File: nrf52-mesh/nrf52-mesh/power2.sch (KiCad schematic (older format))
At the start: 2 parts

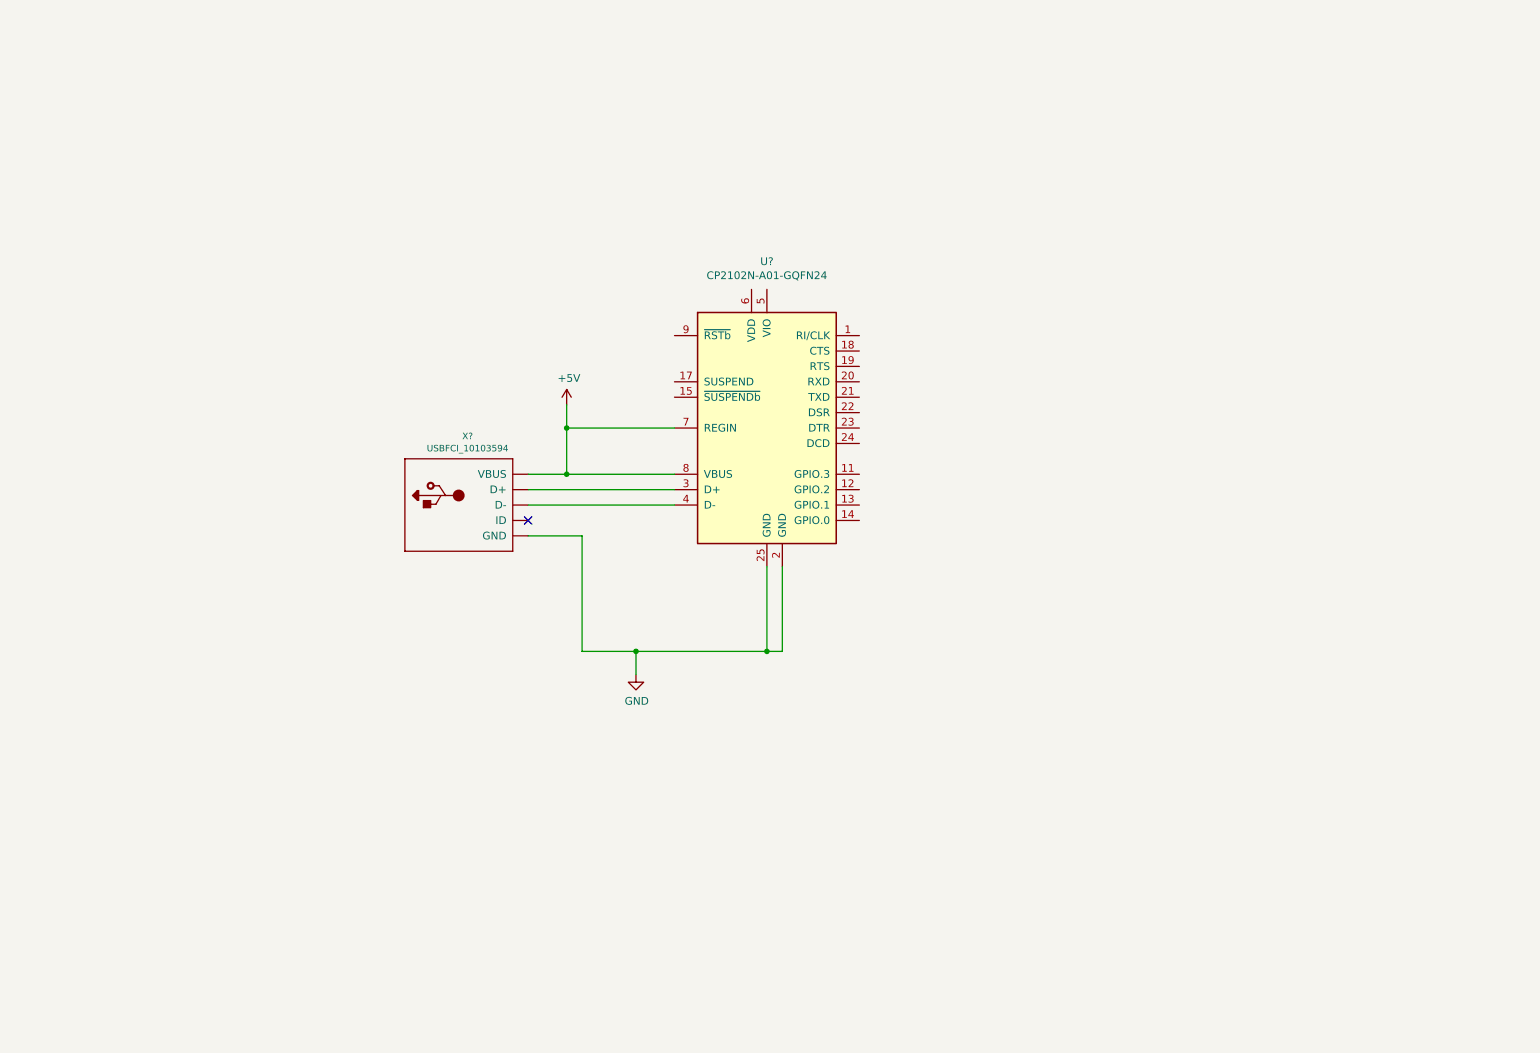
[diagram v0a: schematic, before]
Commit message: CP2102N + MAX1555 + FAN5341 + TPS560200 + TLV62568
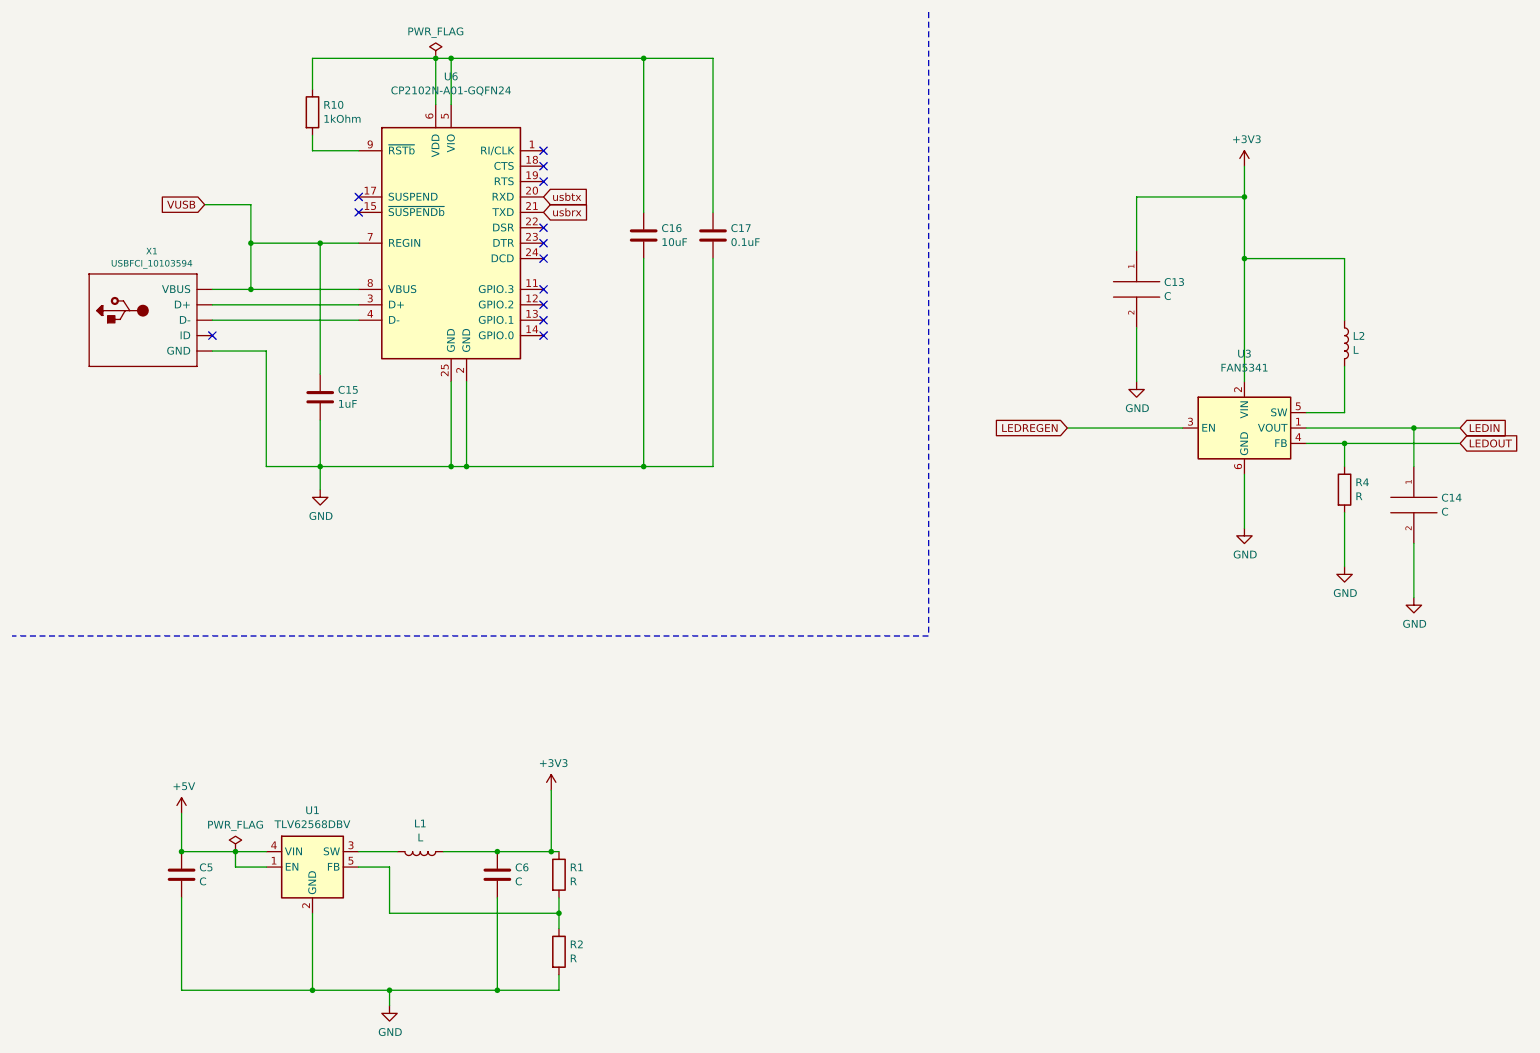
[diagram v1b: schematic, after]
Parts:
- added C13, C14: C, symbol pspice:C
- added C15: 1uF, symbol Device:C
- added C16: 10uF, symbol Device:C
- added C17: 0.1uF, symbol Device:C
- added C5, C6: C, symbol Device:C
- added L1, L2: L, symbol Device:L
- added R1, R2, R4: R, symbol Device:R
- added R10: 1kOhm, symbol Device:R
- added U1: TLV62568DBV, Package_TO_SOT_SMD:SOT-23-5, symbol Regulator_Switching:TLV62568DBV
- added U3: FAN5341, kifootp:FAN5341, symbol kilib:FAN5341
- X1: renamed from X?; footprint (none) -> kifootp:FCI_10103594_MILL
- gave numbers to parts that had none: 1
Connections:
- net +5V: now also C5.1, U1.1 (EN), U1.4 (VIN); no longer U6.7 (REGIN), U6.8 (VBUS), X1.VBUS
- net GND: now also C13.2, C14.2, C15.2, C16.2, C17.2, C5.2, C6.2, R2.2, R4.2, U1.2 (GND), U3.6 (GND)
- net usbtx: now reaches U6.20 (RXD)
- net usbrx: now reaches U6.21 (TXD)
- net at U6.5 (VIO): now also U6.6 (VDD), C16.1, C17.1, R10.1
- net at U6.9 (~RSTb): now also R10.2
- new net: L1.2, U1.3 (SW)
- new net: R1.2, R2.1, U1.5 (FB)
- new net: L2.2, U3.5 (SW)
- new net +3V3: C13.1, C6.1, L1.1, L2.1, R1.1, U3.2 (VIN)
- new net LEDIN: C14.1, U3.1 (VOUT)
- new net LEDOUT: R4.1, U3.4 (FB)
- new net LEDREGEN: U3.3 (EN)
- new net VUSB: C15.1, U6.7 (REGIN), U6.8 (VBUS), X1.VBUS
- no-connect marks 1 -> 13
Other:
- moved on the sheet: U6, X1

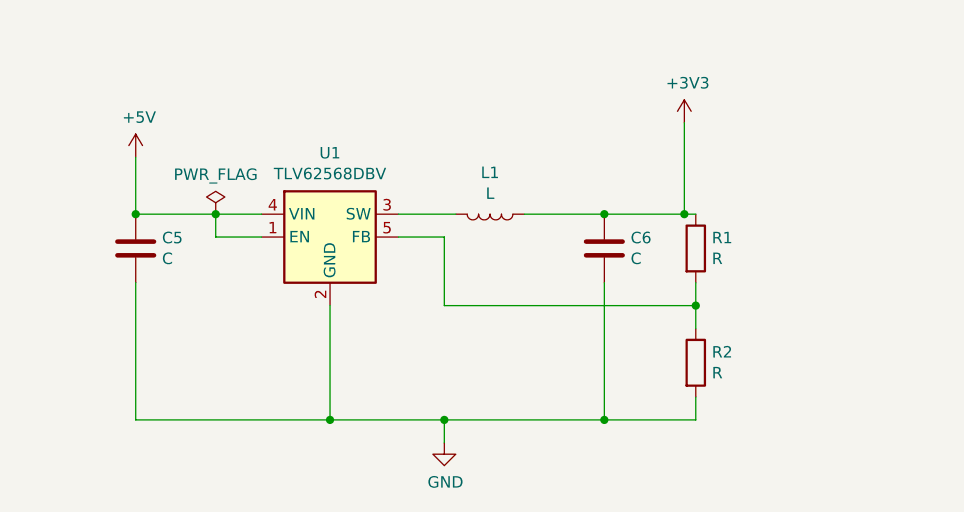
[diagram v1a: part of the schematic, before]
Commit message: CP2102N + MAX1555 + FAN5341 + TPS560200 + TLV62568
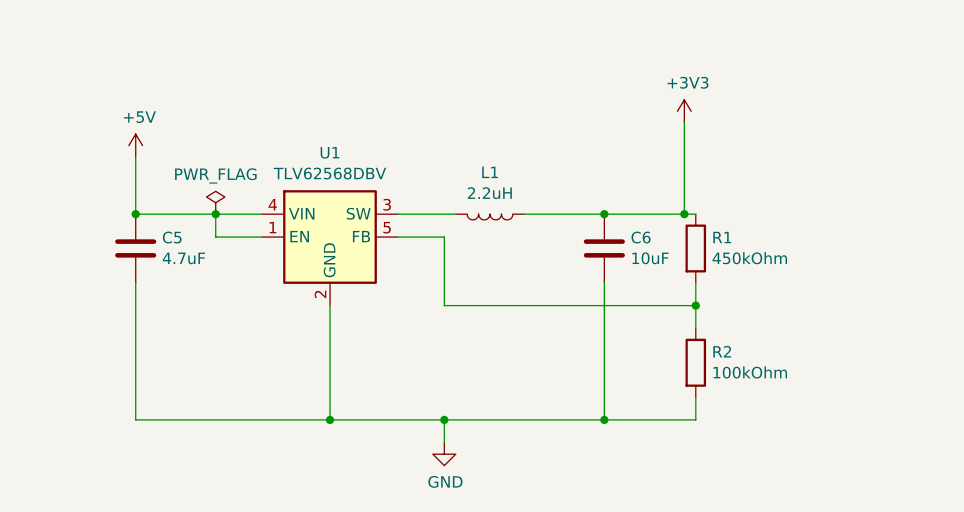
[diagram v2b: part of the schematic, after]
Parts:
- C5: value C -> 4.7uF
- C6: value C -> 10uF
- L1: value L -> 2.2uH
- R1: value R -> 450kOhm
- R2: value R -> 100kOhm
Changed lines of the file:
@@
 AR Path="/5E4F8472/5E5B7E4C" Ref="C5"  Part="1"
 F 0 "C5" H 1765 6196 50  0000 L CNN
-F 1 "C" H 1765 6105 50  0000 L CNN
+F 1 "4.7uF" H 1765 6105 50  0000 L CNN
 F 2 "" H 1688 6000 50  0001 C CNN
 F 3 "~" H 1650 6150 50  0001 C CNN
@@
 AR Path="/5E4F8472/5E5B7E52" Ref="L1"  Part="1"
 F 0 "L1" V 3019 6000 50  0000 C CNN
-F 1 "L" V 3110 6000 50  0000 C CNN
+F 1 "2.2uH" V 3110 6000 50  0000 C CNN
 F 2 "" H 3200 6000 50  0001 C CNN
 F 3 "~" H 3200 6000 50  0001 C CNN
@@
 AR Path="/5E4F8472/5E5B7E58" Ref="C6"  Part="1"
 F 0 "C6" H 3815 6196 50  0000 L CNN
-F 1 "C" H 3815 6105 50  0000 L CNN
+F 1 "10uF" H 3815 6105 50  0000 L CNN
 F 2 "" H 3738 6000 50  0001 C CNN
 F 3 "~" H 3700 6150 50  0001 C CNN
@@
 AR Path="/5E4F8472/5E5B7E5E" Ref="R1"  Part="1"
 F 0 "R1" H 4170 6196 50  0000 L CNN
-F 1 "R" H 4170 6105 50  0000 L CNN
+F 1 "450kOhm" H 4170 6105 50  0000 L CNN
 F 2 "" V 4030 6150 50  0001 C CNN
 F 3 "~" H 4100 6150 50  0001 C CNN
@@
 AR Path="/5E4F8472/5E5B7E64" Ref="R2"  Part="1"
 F 0 "R2" H 4170 6696 50  0000 L CNN
-F 1 "R" H 4170 6605 50  0000 L CNN
+F 1 "100kOhm" H 4170 6605 50  0000 L CNN
 F 2 "" V 4030 6650 50  0001 C CNN
 F 3 "~" H 4100 6650 50  0001 C CNN

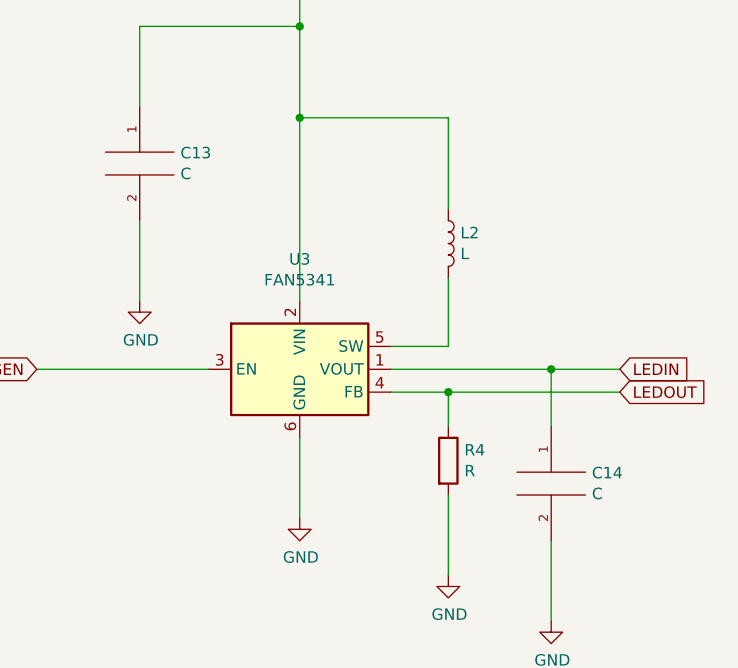
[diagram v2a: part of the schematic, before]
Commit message: CP2102N + MAX1555 + FAN5341 + TPS560200 + TLV62568
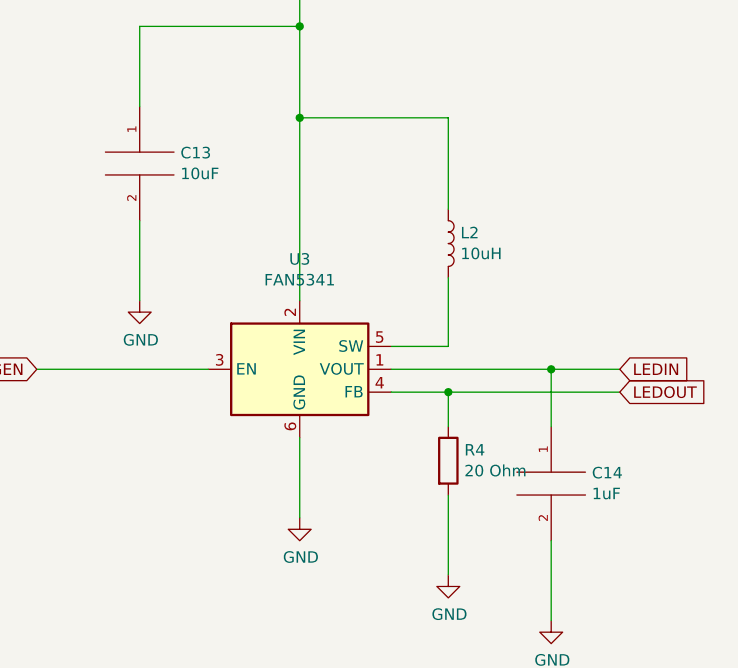
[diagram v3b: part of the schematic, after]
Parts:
- C13: value C -> 10uF; footprint (none) -> Capacitor_SMD:C_0603_1608Metric
- C14: value C -> 1uF; footprint (none) -> Capacitor_SMD:C_0402_1005Metric
- C15, C17, C5, C6: footprint (none) -> Capacitor_SMD:C_0402_1005Metric
- C16: footprint (none) -> Capacitor_SMD:C_0603_1608Metric
- L2: value L -> 10uH
- R1, R10, R2: footprint (none) -> Resistor_SMD:R_0402_1005Metric
- R4: value R -> 20 Ohm; footprint (none) -> Resistor_SMD:R_0402_1005Metric
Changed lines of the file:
@@
 F 0 "C5" H 1765 6196 50  0000 L CNN
 F 1 "4.7uF" H 1765 6105 50  0000 L CNN
-F 2 "" H 1688 6000 50  0001 C CNN
+F 2 "Capacitor_SMD:C_0402_1005Metric" H 1688 6000 50  0001 C CNN
 F 3 "~" H 1650 6150 50  0001 C CNN
 	1    1650 6150
@@
 F 0 "C6" H 3815 6196 50  0000 L CNN
 F 1 "10uF" H 3815 6105 50  0000 L CNN
-F 2 "" H 3738 6000 50  0001 C CNN
+F 2 "Capacitor_SMD:C_0402_1005Metric" H 3738 6000 50  0001 C CNN
 F 3 "~" H 3700 6150 50  0001 C CNN
 	1    3700 6150
@@
 F 0 "R1" H 4170 6196 50  0000 L CNN
 F 1 "450kOhm" H 4170 6105 50  0000 L CNN
-F 2 "" V 4030 6150 50  0001 C CNN
+F 2 "Resistor_SMD:R_0402_1005Metric" V 4030 6150 50  0001 C CNN
 F 3 "~" H 4100 6150 50  0001 C CNN
 	1    4100 6150
@@
 F 0 "R2" H 4170 6696 50  0000 L CNN
 F 1 "100kOhm" H 4170 6605 50  0000 L CNN
-F 2 "" V 4030 6650 50  0001 C CNN
+F 2 "Resistor_SMD:R_0402_1005Metric" V 4030 6650 50  0001 C CNN
 F 3 "~" H 4100 6650 50  0001 C CNN
 	1    4100 6650
@@
 AR Path="/5E4F8472/5E5C2A77" Ref="C14"  Part="1"
 F 0 "C14" H 9828 3796 50  0000 L CNN
-F 1 "C" H 9828 3705 50  0000 L CNN
-F 2 "" H 9650 3750 50  0001 C CNN
+F 1 "1uF" H 9828 3705 50  0000 L CNN
+F 2 "Capacitor_SMD:C_0402_1005Metric" H 9650 3750 50  0001 C CNN
 F 3 "~" H 9650 3750 50  0001 C CNN
 	1    9650 3750
@@
 AR Path="/5E4F8472/5E5C2A7D" Ref="R4"  Part="1"
 F 0 "R4" H 9270 3696 50  0000 L CNN
-F 1 "R" H 9270 3605 50  0000 L CNN
-F 2 "" V 9130 3650 50  0001 C CNN
+F 1 "20 Ohm" H 9270 3605 50  0000 L CNN
+F 2 "Resistor_SMD:R_0402_1005Metric" V 9130 3650 50  0001 C CNN
 F 3 "~" H 9200 3650 50  0001 C CNN
 	1    9200 3650
@@
 AR Path="/5E4F8472/5E5C2A9B" Ref="C13"  Part="1"
 F 0 "C13" H 8028 2396 50  0000 L CNN
-F 1 "C" H 8028 2305 50  0000 L CNN
-F 2 "" H 7850 2350 50  0001 C CNN
+F 1 "10uF" H 8028 2305 50  0000 L CNN
+F 2 "Capacitor_SMD:C_0603_1608Metric" H 7850 2350 50  0001 C CNN
 F 3 "~" H 7850 2350 50  0001 C CNN
 	1    7850 2350
@@
 AR Path="/5E4F8472/5E5C2AA1" Ref="L2"  Part="1"
 F 0 "L2" H 9253 2746 50  0000 L CNN
-F 1 "L" H 9253 2655 50  0000 L CNN
+F 1 "10uH" H 9253 2655 50  0000 L CNN
 F 2 "" H 9200 2700 50  0001 C CNN
 F 3 "~" H 9200 2700 50  0001 C CNN
@@
 F 0 "R10" H 2570 1246 50  0000 L CNN
 F 1 "1kOhm" H 2570 1155 50  0000 L CNN
-F 2 "" V 2430 1200 50  0001 C CNN
+F 2 "Resistor_SMD:R_0402_1005Metric" V 2430 1200 50  0001 C CNN
 F 3 "~" H 2500 1200 50  0001 C CNN
 	1    2500 1200
@@
 F 0 "C15" H 2665 3096 50  0000 L CNN
 F 1 "1uF" H 2665 3005 50  0000 L CNN
-F 2 "" H 2588 2900 50  0001 C CNN
+F 2 "Capacitor_SMD:C_0402_1005Metric" H 2588 2900 50  0001 C CNN
 F 3 "~" H 2550 3050 50  0001 C CNN
 	1    2550 3050
@@
 F 0 "C16" H 4765 2046 50  0000 L CNN
 F 1 "10uF" H 4765 1955 50  0000 L CNN
-F 2 "" H 4688 1850 50  0001 C CNN
+F 2 "Capacitor_SMD:C_0603_1608Metric" H 4688 1850 50  0001 C CNN
 F 3 "~" H 4650 2000 50  0001 C CNN
 	1    4650 2000
@@
 F 0 "C17" H 5215 2046 50  0000 L CNN
 F 1 "0.1uF" H 5215 1955 50  0000 L CNN
-F 2 "" H 5138 1850 50  0001 C CNN
+F 2 "Capacitor_SMD:C_0402_1005Metric" H 5138 1850 50  0001 C CNN
 F 3 "~" H 5100 2000 50  0001 C CNN
 	1    5100 2000

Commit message: CP2102N + MAX1555 + FAN5341 + TPS560200 + TLV62568
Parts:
- L1, L2: footprint (none) -> Inductor_SMD:L_0805_2012Metric
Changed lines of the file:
@@
 F 0 "L1" V 3019 6000 50  0000 C CNN
 F 1 "2.2uH" V 3110 6000 50  0000 C CNN
-F 2 "" H 3200 6000 50  0001 C CNN
+F 2 "Inductor_SMD:L_0805_2012Metric" H 3200 6000 50  0001 C CNN
 F 3 "~" H 3200 6000 50  0001 C CNN
 	1    3200 6000
@@
 F 0 "L2" H 9253 2746 50  0000 L CNN
 F 1 "10uH" H 9253 2655 50  0000 L CNN
-F 2 "" H 9200 2700 50  0001 C CNN
+F 2 "Inductor_SMD:L_0805_2012Metric" H 9200 2700 50  0001 C CNN
 F 3 "~" H 9200 2700 50  0001 C CNN
 	1    9200 2700

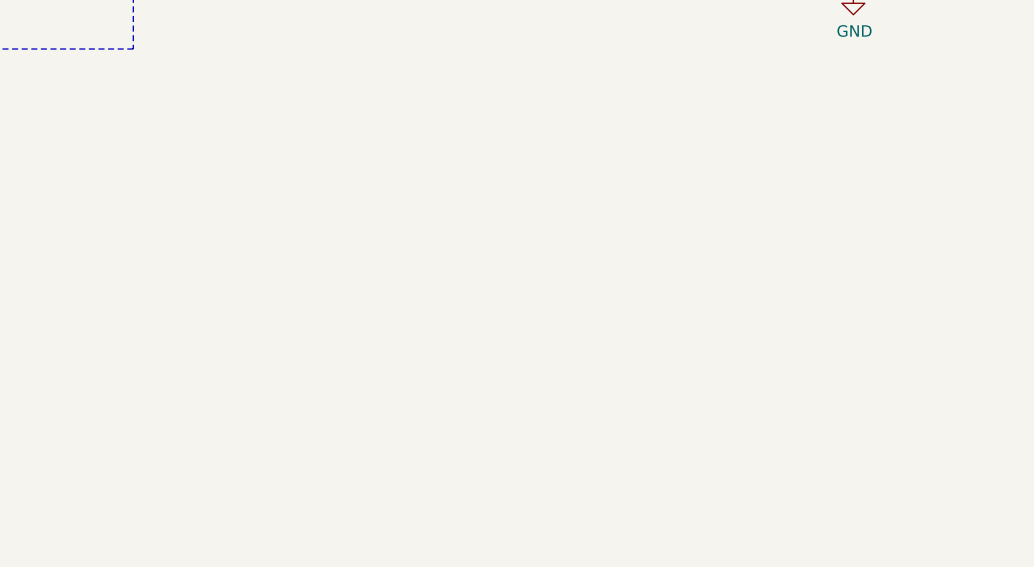
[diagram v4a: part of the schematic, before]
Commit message: CP2102N + MAX1555 + FAN5341 + TPS560200 + TLV62568
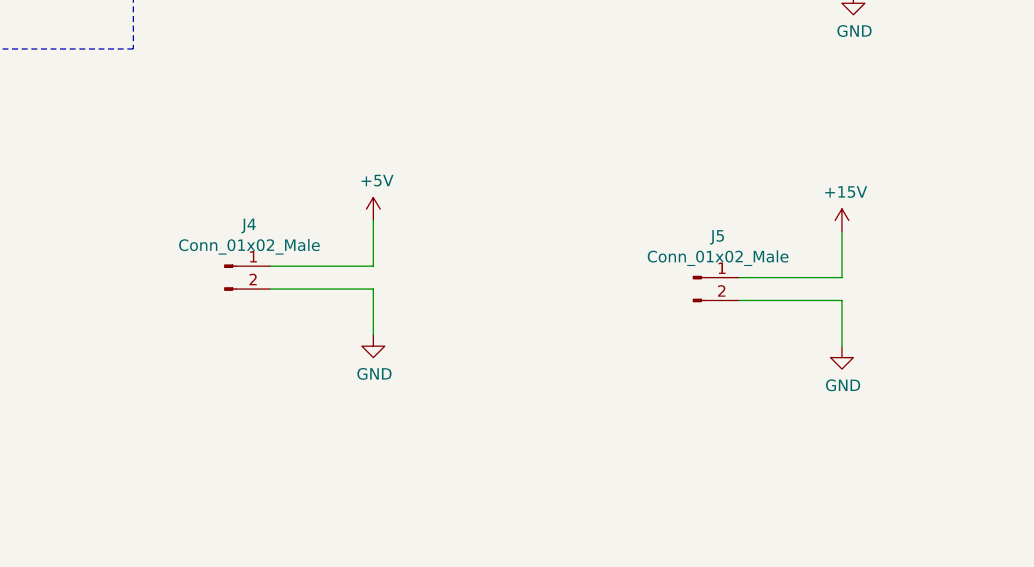
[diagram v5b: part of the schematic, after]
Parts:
- added J4, J5: Conn_01x02_Male, Connector_PinHeader_2.54mm:PinHeader_1x02_P2.54mm_Vertical, symbol Connector:Conn_01x02_Male
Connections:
- net +5V: now also J4.1 (Pin_1)
- net GND: now also J4.2 (Pin_2), J5.2 (Pin_2)
- new net +15V: J5.1 (Pin_1)
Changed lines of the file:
@@
+	1    0    0    -1
+$EndComp
+$Comp
+L Connector:Conn_01x02_Male J4
+U 1 1 5E638311
+P 6900 5550
+F 0 "J4" H 7008 5731 50  0000 C CNN
+F 1 "Conn_01x02_Male" H 7008 5640 50  0000 C CNN
+F 2 "Connector_PinHeader_2.54mm:PinHeader_1x02_P2.54mm_Vertical" H 6900 5550 50  0001 C CNN
+F 3 "~" H 6900 5550 50  0001 C CNN
+	1    6900 5550
+	1    0    0    -1
+$EndComp
+$Comp
+L power:+5V #PWR036
+U 1 1 5E6396BF
+P 7550 5350
+F 0 "#PWR036" H 7550 5200 50  0001 C CNN
+F 1 "+5V" H 7565 5523 50  0000 C CNN
+F 2 "" H 7550 5350 50  0001 C CNN
+F 3 "" H 7550 5350 50  0001 C CNN
+	1    7550 5350
+	1    0    0    -1
+$EndComp
+$Comp
+L power:GND #PWR037
+U 1 1 5E63A80C
+P 7550 5850
+F 0 "#PWR037" H 7550 5600 50  0001 C CNN
+F 1 "GND" H 7555 5677 50  0000 C CNN
+F 2 "" H 7550 5850 50  0001 C CNN
+F 3 "" H 7550 5850 50  0001 C CNN
+	1    7550 5850
+	1    0    0    -1
+$EndComp
+Wire Wire Line
+	7100 5550 7550 5550
+Wire Wire Line
+	7550 5550 7550 5350
+Wire Wire Line
+	7100 5650 7550 5650
+Wire Wire Line
+	7550 5650 7550 5850
+$Comp
+L Connector:Conn_01x02_Male J5
+U 1 1 5E653952
+P 8950 5600
+F 0 "J5" H 9058 5781 50  0000 C CNN
+F 1 "Conn_01x02_Male" H 9058 5690 50  0000 C CNN
+F 2 "Connector_PinHeader_2.54mm:PinHeader_1x02_P2.54mm_Vertical" H 8950 5600 50  0001 C CNN
+F 3 "~" H 8950 5600 50  0001 C CNN
+	1    8950 5600
+	1    0    0    -1
+$EndComp
+$Comp
+L power:GND #PWR039
+U 1 1 5E65395E
+P 9600 5900
+F 0 "#PWR039" H 9600 5650 50  0001 C CNN
+F 1 "GND" H 9605 5727 50  0000 C CNN
+F 2 "" H 9600 5900 50  0001 C CNN
+F 3 "" H 9600 5900 50  0001 C CNN
+	1    9600 5900
+	1    0    0    -1
+$EndComp
+Wire Wire Line
+	9150 5600 9600 5600
+Wire Wire Line
+	9600 5600 9600 5400
+Wire Wire Line
+	9150 5700 9600 5700
+Wire Wire Line
+	9600 5700 9600 5900
+$Comp
+L power:+15V #PWR038
+U 1 1 5E655B8D
+P 9600 5400
+F 0 "#PWR038" H 9600 5250 50  0001 C CNN
+F 1 "+15V" H 9615 5573 50  0000 C CNN
+F 2 "" H 9600 5400 50  0001 C CNN
+F 3 "" H 9600 5400 50  0001 C CNN
+	1    9600 5400
 	1    0    0    -1
 $EndComp
